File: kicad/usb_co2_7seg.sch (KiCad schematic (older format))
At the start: 14 parts, among them U1 PinHeader_XIAO, U2 PinHeader_XIAO, U3 SeeeduinoXIAO, U4 MH-Z19B, U5 TM1637, U6 7segment_led, U7 SW_push_2pin

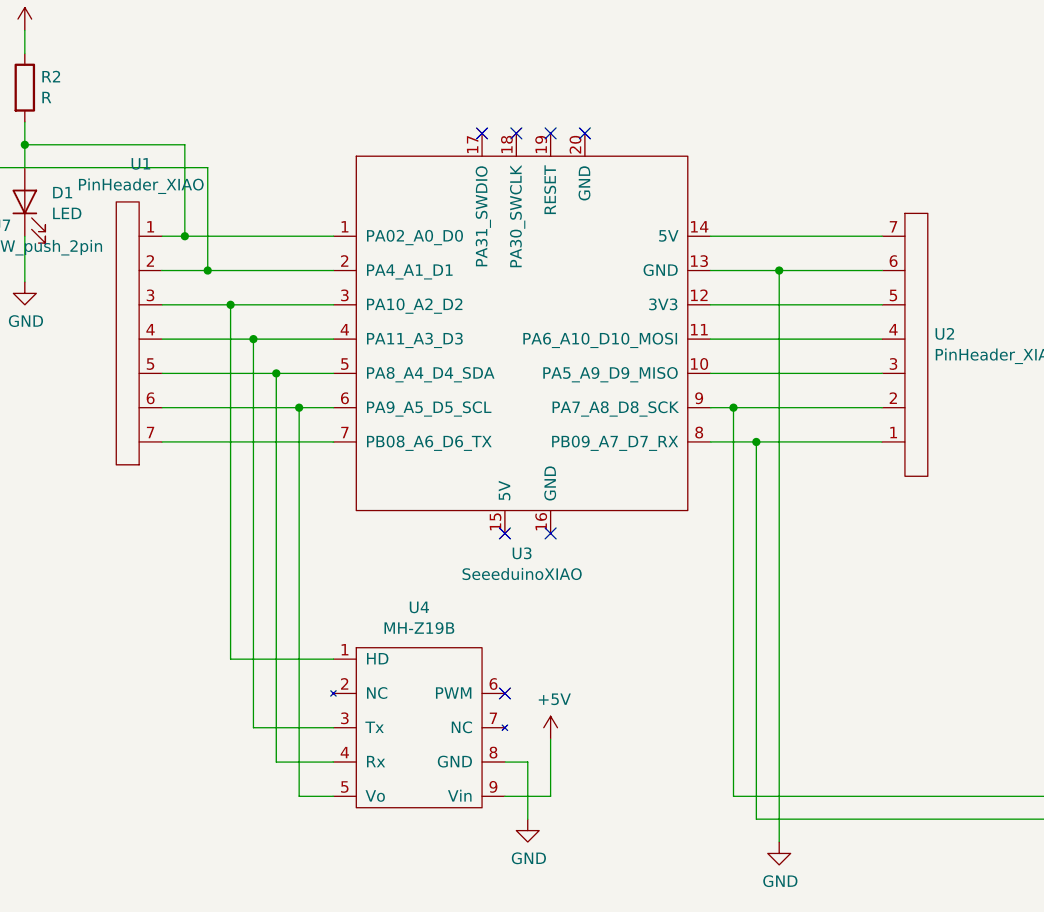
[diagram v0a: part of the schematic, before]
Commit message: ファイル名を修正
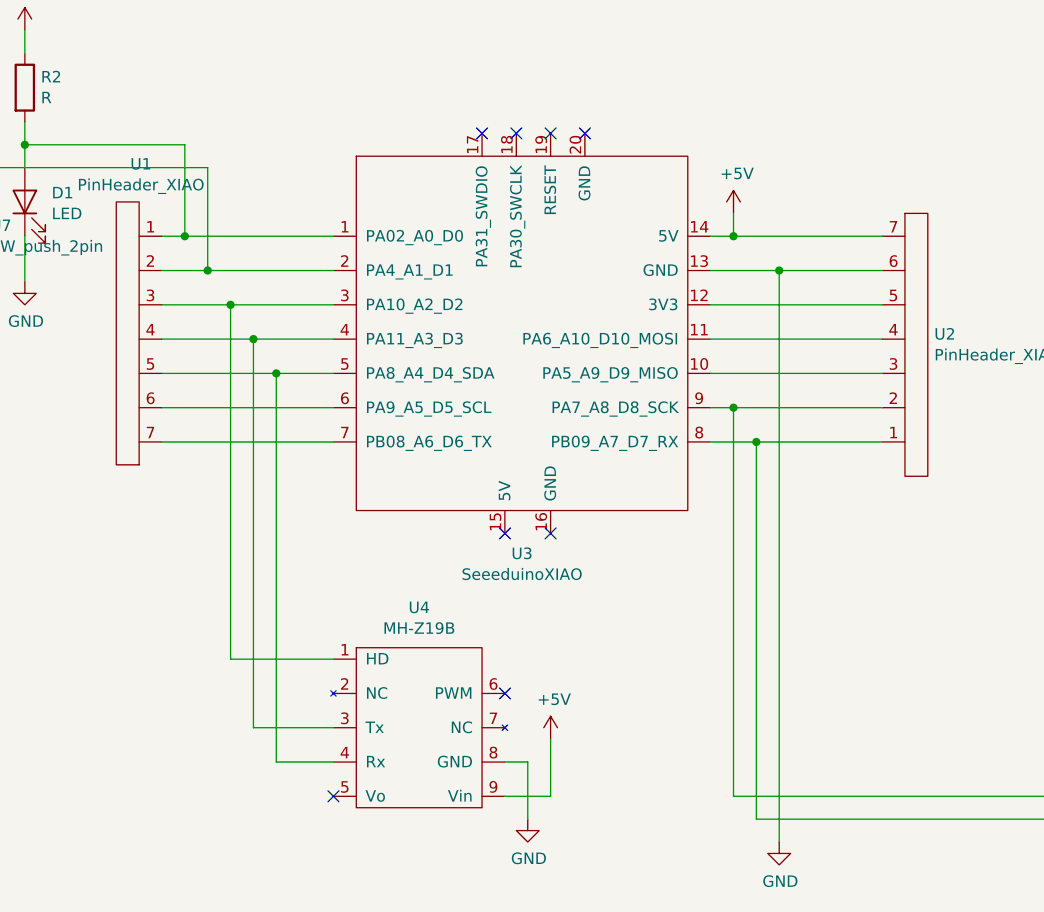
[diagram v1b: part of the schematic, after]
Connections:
- net +5V: now also U2.7, U3.14 (5V)
- net at U1.6, U3.6 (PA9_A5_D5_SCL): no longer U4.5 (Vo)
- no-connect marks 11 -> 12
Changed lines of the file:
@@
 EESchema Schematic File Version 4
-LIBS:usb_soil_moisture-cache
 EELAYER 29 0
 EELAYER END
@@
 $EndComp
 $Comp
-L kicad_mylib:MH-Z19B U4
-U 1 1 60785EDD
-P 2550 4450
-F 0 "U4" H 2925 4675 50  0000 C CNN
-F 1 "MH-Z19B" H 2925 4584 50  0000 C CNN
-F 2 "kicad_mylib:MH-Z19B" H 2650 4550 50  0001 C CNN
-F 3 "" H 2650 4550 50  0001 C CNN
-	1    2550 4450
-	1    0    0    -1
-$EndComp
-$Comp
-L kicad_mylib:TM1637 U5
-U 1 1 6078679C
-P 6850 4150
-F 0 "U5" H 7175 5865 50  0000 C CNN
-F 1 "TM1637" H 7175 5774 50  0000 C CNN
-F 2 "kicad_mylib:TM1630" H 6900 5750 50  0001 C CNN
-F 3 "" H 6900 5750 50  0001 C CNN
-	1    6850 4150
-	1    0    0    -1
-$EndComp
-$Comp
 L kicad_mylib:7segment_led U6
 U 1 1 60787049
@@
 $EndComp
 Wire Wire Line
-	4950 2600 4200 2600
+	4950 2600 4300 2600
 $Comp
 L kicad_mylib:PinHeader_XIAO U2
@@
 Wire Wire Line
 	2550 4450 2100 4450
-Wire Wire Line
-	2550 5050 2400 5050
-Wire Wire Line
-	2400 5050 2400 3350
-Wire Wire Line
-	2550 3350 2400 3350
-Wire Wire Line
-	2400 3350 1800 3350
-Connection ~ 2400 3350
 Wire Wire Line
 	7600 3000 8050 3000
@@
 Wire Wire Line
 	2000 2750 2550 2750
+Wire Wire Line
+	1800 3350 2550 3350
+NoConn ~ 2550 5050
+$Comp
+L power:+5V #PWR01
+U 1 1 608CEBC4
+P 4300 2500
+F 0 "#PWR01" H 4300 2350 50  0001 C CNN
+F 1 "+5V" H 4315 2673 50  0000 C CNN
+F 2 "" H 4300 2500 50  0001 C CNN
+F 3 "" H 4300 2500 50  0001 C CNN
+	1    4300 2500
+	1    0    0    -1
+$EndComp
+Wire Wire Line
+	4300 2500 4300 2600
+Connection ~ 4300 2600
+Wire Wire Line
+	4300 2600 4200 2600
+$Comp
+L kicad_mylib:MH-Z19B U4
+U 1 1 609198A9
+P 2550 4450
+F 0 "U4" H 2925 4675 50  0000 C CNN
+F 1 "MH-Z19B" H 2925 4584 50  0000 C CNN
+F 2 "kicad_mylib:MH-Z19B" H 2650 4550 50  0001 C CNN
+F 3 "" H 2650 4550 50  0001 C CNN
+	1    2550 4450
+	1    0    0    -1
+$EndComp
+$Comp
+L kicad_mylib:TM1637 U5
+U 1 1 6091AFF2
+P 6850 4150
+F 0 "U5" H 7175 5865 50  0000 C CNN
+F 1 "TM1637" H 7175 5774 50  0000 C CNN
+F 2 "kicad_mylib:TM1630" H 6900 5750 50  0001 C CNN
+F 3 "" H 6900 5750 50  0001 C CNN
+	1    6850 4150
+	1    0    0    -1
+$EndComp
 $EndSCHEMATC

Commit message: MH-Z14Aに対応 ERC OK
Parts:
- added U8: MH-Z14A, kicad_mylib:MH-Z14A, symbol kicad_mylib:MH-Z14A
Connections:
- wire segments 137 -> 163
- no-connect marks 12 -> 21
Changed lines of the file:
@@
 	2550 2900 2100 2900
 Wire Wire Line
-	2100 4450 2100 2900
+	2100 4450 2100 4150
 Connection ~ 2100 2900
 Wire Wire Line
@@
 	1    0    0    -1
 $EndComp
+$Comp
+L kicad_mylib:MH-Z14A U8
+U 1 1 60C66D31
+P 2400 5650
+F 0 "U8" H 2975 5915 50  0000 C CNN
+F 1 "MH-Z14A" H 2975 5824 50  0000 C CNN
+F 2 "kicad_mylib:MH-Z14A" H 2550 5800 50  0001 C CNN
+F 3 "" H 2550 5800 50  0001 C CNN
+	1    2400 5650
+	1    0    0    -1
+$EndComp
+Wire Wire Line
+	2400 5750 2300 5750
+Wire Wire Line
+	2300 5750 2300 4900
+Connection ~ 2300 4900
+Wire Wire Line
+	2400 5650 2200 5650
+Wire Wire Line
+	2200 5650 2200 4750
+Connection ~ 2200 4750
+$Comp
+L power:+5V #PWR03
+U 1 1 60C7A267
+P 3750 5350
+F 0 "#PWR03" H 3750 5200 50  0001 C CNN
+F 1 "+5V" H 3765 5523 50  0000 C CNN
+F 2 "" H 3750 5350 50  0001 C CNN
+F 3 "" H 3750 5350 50  0001 C CNN
+	1    3750 5350
+	1    0    0    -1
+$EndComp
+$Comp
+L power:GND #PWR02
+U 1 1 60C7A8E0
+P 3650 6950
+F 0 "#PWR02" H 3650 6700 50  0001 C CNN
+F 1 "GND" H 3655 6777 50  0000 C CNN
+F 2 "" H 3650 6950 50  0001 C CNN
+F 3 "" H 3650 6950 50  0001 C CNN
+	1    3650 6950
+	1    0    0    -1
+$EndComp
+Wire Wire Line
+	3550 6050 3650 6050
+Wire Wire Line
+	3550 5950 3750 5950
+Wire Wire Line
+	3550 6550 3650 6550
+Wire Wire Line
+	3650 6550 3650 6750
+Wire Wire Line
+	2400 5950 2300 5950
+Wire Wire Line
+	2300 5950 2300 6150
+Wire Wire Line
+	2300 6750 3650 6750
+Connection ~ 3650 6750
+Wire Wire Line
+	3650 6750 3650 6950
+Wire Wire Line
+	2400 6150 2300 6150
+Connection ~ 2300 6150
+Wire Wire Line
+	2300 6150 2300 6750
+NoConn ~ 3550 5750
+NoConn ~ 3550 5850
+NoConn ~ 3550 6150
+NoConn ~ 3550 6250
+NoConn ~ 3550 6450
+Wire Wire Line
+	3750 5350 3750 5400
+Wire Wire Line
+	2100 5400 3750 5400
+Connection ~ 3750 5400
+Wire Wire Line
+	3750 5400 3750 5950
+Wire Wire Line
+	2100 5400 2100 5850
+Connection ~ 2100 5850
+Wire Wire Line
+	2100 5850 2100 6050
+NoConn ~ 2400 6250
+NoConn ~ 2400 6350
+NoConn ~ 2400 6450
+NoConn ~ 2400 6550
+Connection ~ 3650 6550
+Wire Wire Line
+	3650 6050 3650 6550
+Wire Wire Line
+	2100 6050 2400 6050
+Wire Wire Line
+	2100 5850 2400 5850
+Wire Wire Line
+	3550 6350 3850 6350
+Wire Wire Line
+	3850 6350 3850 4150
+Wire Wire Line
+	3850 4150 2100 4150
+Connection ~ 2100 4150
+Wire Wire Line
+	2100 4150 2100 2900
 $EndSCHEMATC

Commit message: MH-Z14Aの不要なピンを未接続にした
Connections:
- wire segments 163 -> 149
- no-connect marks 21 -> 26
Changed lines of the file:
@@
 	1200 2200 1200 2300
-Wire Wire Line
-	900  2300 2000 2300
 Wire Wire Line
 	1800 2750 2000 2750
@@
 L power:+5V #PWR03
 U 1 1 60C7A267
-P 3750 5350
-F 0 "#PWR03" H 3750 5200 50  0001 C CNN
-F 1 "+5V" H 3765 5523 50  0000 C CNN
-F 2 "" H 3750 5350 50  0001 C CNN
-F 3 "" H 3750 5350 50  0001 C CNN
-	1    3750 5350
+P 2100 5900
+F 0 "#PWR03" H 2100 5750 50  0001 C CNN
+F 1 "+5V" H 2115 6073 50  0000 C CNN
+F 2 "" H 2100 5900 50  0001 C CNN
+F 3 "" H 2100 5900 50  0001 C CNN
+	1    2100 5900
 	1    0    0    -1
 $EndComp
@@
 L power:GND #PWR02
 U 1 1 60C7A8E0
-P 3650 6950
-F 0 "#PWR02" H 3650 6700 50  0001 C CNN
-F 1 "GND" H 3655 6777 50  0000 C CNN
-F 2 "" H 3650 6950 50  0001 C CNN
-F 3 "" H 3650 6950 50  0001 C CNN
-	1    3650 6950
+P 2300 7000
+F 0 "#PWR02" H 2300 6750 50  0001 C CNN
+F 1 "GND" H 2305 6827 50  0000 C CNN
+F 2 "" H 2300 7000 50  0001 C CNN
+F 3 "" H 2300 7000 50  0001 C CNN
+	1    2300 7000
 	1    0    0    -1
 $EndComp
 Wire Wire Line
-	3550 6050 3650 6050
-Wire Wire Line
-	3550 5950 3750 5950
-Wire Wire Line
-	3550 6550 3650 6550
-Wire Wire Line
-	3650 6550 3650 6750
-Wire Wire Line
-	2400 5950 2300 5950
-Wire Wire Line
-	2300 5950 2300 6150
-Wire Wire Line
-	2300 6750 3650 6750
-Connection ~ 3650 6750
-Wire Wire Line
-	3650 6750 3650 6950
-Wire Wire Line
 	2400 6150 2300 6150
-Connection ~ 2300 6150
-Wire Wire Line
-	2300 6150 2300 6750
 NoConn ~ 3550 5750
 NoConn ~ 3550 5850
@@
 NoConn ~ 3550 6250
 NoConn ~ 3550 6450
-Wire Wire Line
-	3750 5350 3750 5400
-Wire Wire Line
-	2100 5400 3750 5400
-Connection ~ 3750 5400
-Wire Wire Line
-	3750 5400 3750 5950
-Wire Wire Line
-	2100 5400 2100 5850
-Connection ~ 2100 5850
-Wire Wire Line
-	2100 5850 2100 6050
 NoConn ~ 2400 6250
 NoConn ~ 2400 6350
 NoConn ~ 2400 6450
 NoConn ~ 2400 6550
-Connection ~ 3650 6550
-Wire Wire Line
-	3650 6050 3650 6550
 Wire Wire Line
 	2100 6050 2400 6050
-Wire Wire Line
-	2100 5850 2400 5850
 Wire Wire Line
 	3550 6350 3850 6350
@@
 Wire Wire Line
 	2100 4150 2100 2900
+Wire Wire Line
+	900  2300 2000 2300
+Wire Wire Line
+	2100 5900 2100 6050
+Wire Wire Line
+	2300 6150 2300 7000
+NoConn ~ 2400 5950
+NoConn ~ 2400 5850
+NoConn ~ 3550 6050
+NoConn ~ 3550 5950
+NoConn ~ 3550 6550
 $EndSCHEMATC
